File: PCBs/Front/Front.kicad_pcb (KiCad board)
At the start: 2 copper layers, 82 x 64 mm, 0 parts

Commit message: Front silks
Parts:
- added G***: LOGO, LOGO, F.Cu at (129.9, 99.9)

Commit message: front pcb done
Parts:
- added J1: PWR, fp:PinHeader_1x04_P2.54mm_Vertical_SMD_Both, B.Cu at (160.0, 100.0)
- added J2: CAP_TOUCH, fp:PinHeader_1x04_P2.54mm_Vertical_SMD_Both, B.Cu at (100.0, 100.0)

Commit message: Almost final adjustments
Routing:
- added copper zone on B.Cu, net (none)
- added copper zone on F.Cu, net (none)
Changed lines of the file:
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@@
   (gr_curve locked (pts (xy 105.543648 82.812393) (xy 105.668334 82.733995) (xy 105.809543 82.668889) (xy 105.944882 82.614975))
     (stroke (width 0.2) (type solid)) (layer "Edge.Cuts"))
+  (zone (net 0) (net_name "") (layers "F&B.Cu") (hatch edge 0.5)
+    (connect_pads (clearance 0.5))
+    (min_thickness 0.25) (filled_areas_thickness no)
+    (fill yes (thermal_gap 0.5) (thermal_bridge_width 0.5) (island_removal_mode 1) (island_area_min 10))
+    (polygon
+      (pts
+        (xy 180.6 59.6)
+        (xy 180.6 136.1)
+        (xy 180.15 136.55)
+        (xy 78.65 136.55)
+        (xy 77.85 135.75)
+        (xy 77.85 59.6)
+      )
+    )
+  )
 )

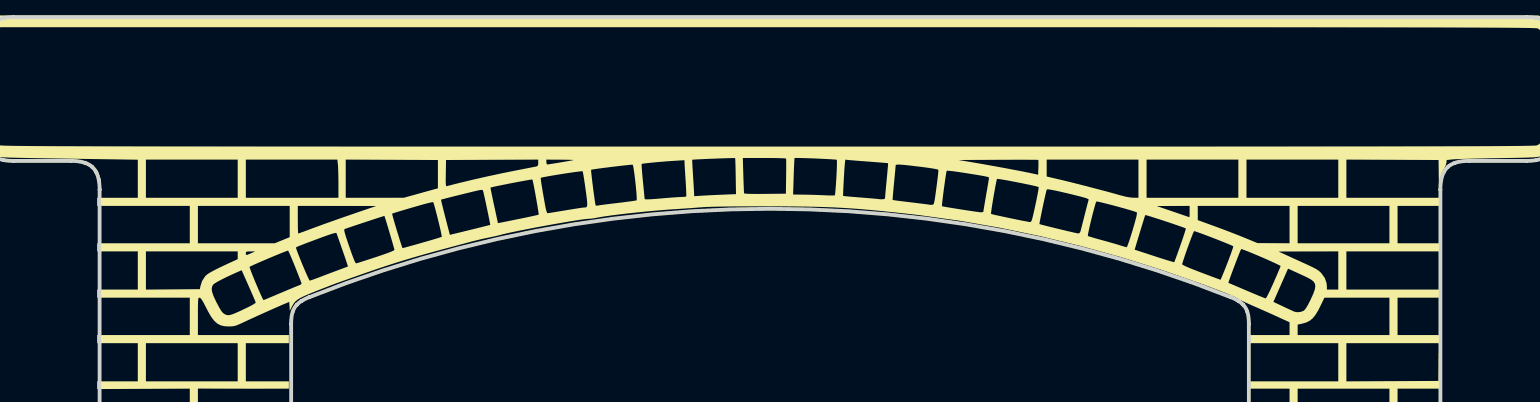
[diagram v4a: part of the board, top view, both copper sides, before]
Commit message: Order num place and gerbers for front
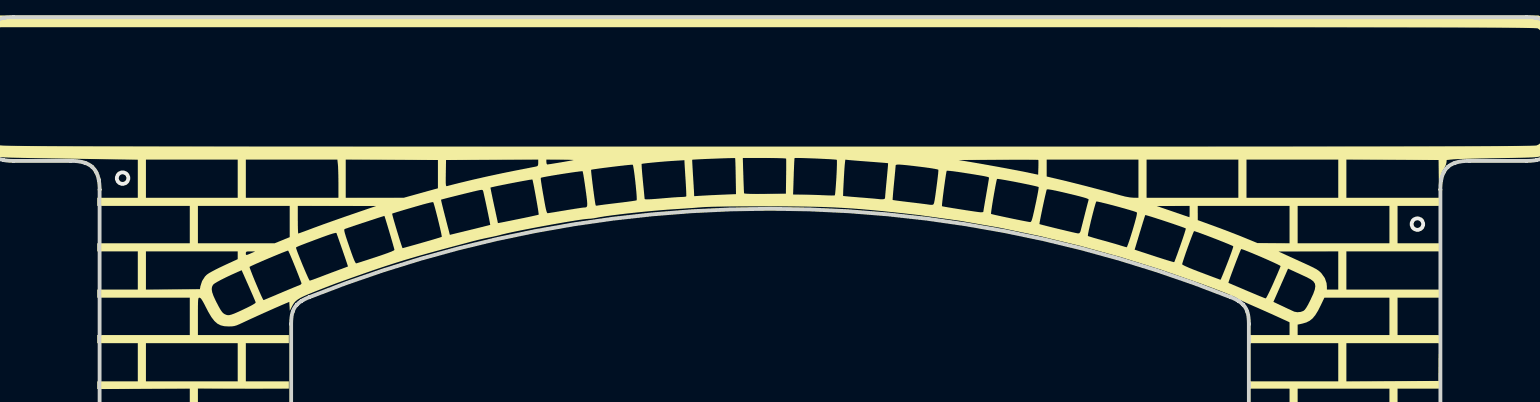
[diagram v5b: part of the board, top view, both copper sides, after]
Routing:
- net (no net): vias 0 -> 2
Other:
- board text added: "JLCJLCJLCJLC"
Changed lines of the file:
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@@
       (disableapertmacros false)
       (usegerberextensions false)
-      (usegerberattributes true)
-      (usegerberadvancedattributes true)
-      (creategerberjobfile true)
+      (usegerberattributes false)
+      (usegerberadvancedattributes false)
+      (creategerberjobfile false)
       (dashed_line_dash_ratio 12.000000)
       (dashed_line_gap_ratio 3.000000)
@@
       (psa4output false)
       (plotreference true)
-      (plotvalue true)
+      (plotvalue false)
       (plotinvisibletext false)
       (sketchpadsonfab false)
-      (subtractmaskfromsilk false)
+      (subtractmaskfromsilk true)
       (outputformat 1)
       (mirror false)
-      (drillshape 1)
+      (drillshape 0)
       (scaleselection 1)
-      (outputdirectory "")
+      (outputdirectory "front_gerbers/")
     )
   )
@@
   (gr_curve locked (pts (xy 105.543648 82.812393) (xy 105.668334 82.733995) (xy 105.809543 82.668889) (xy 105.944882 82.614975))
     (stroke (width 0.2) (type solid)) (layer "Edge.Cuts"))
+  (gr_text "JLCJLCJLCJLC" (at 169.42 130.47) (layer "B.SilkS")
+    (effects (font (size 1 1) (thickness 0.16)) (justify left bottom mirror))
+  )
+  (via (at 163.8 78.8) (size 0.8) (drill 0.4) (layers "F.Cu" "B.Cu") (net 0))
+  (via (at 96.2 76.4) (size 0.8) (drill 0.4) (layers "F.Cu" "B.Cu") (net 0))
   (zone (net 0) (net_name "") (layers "F&B.Cu") (hatch edge 0.5)
     (connect_pads (clearance 0.5))
